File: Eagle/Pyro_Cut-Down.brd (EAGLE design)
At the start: 51.4 x 63.5 mm, 44 parts, among them IC1 ERIC9-FCC, IC2 MCP111T-240E/TT, IC3 SN74LVC2G02DCTR, IC4 MPL3115A2LGA8, Q1 DMG3415U-7, Q2 2N2222

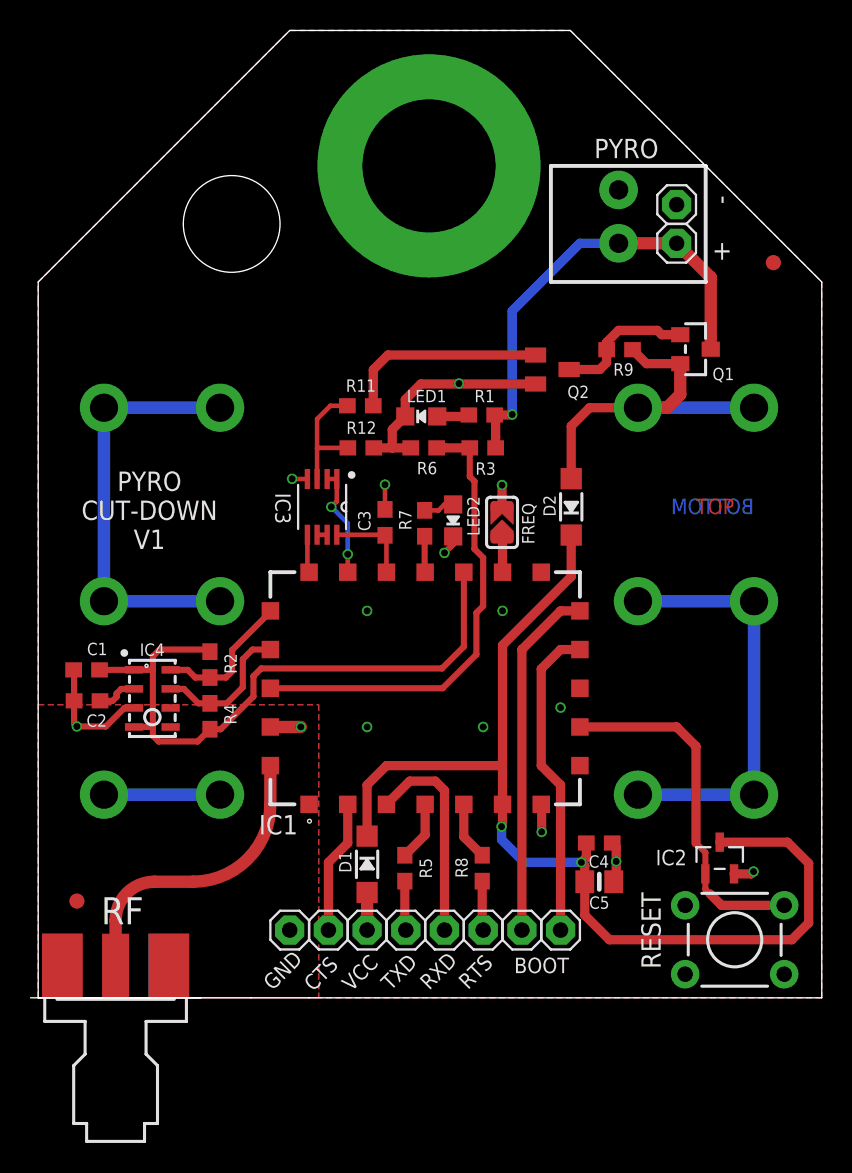
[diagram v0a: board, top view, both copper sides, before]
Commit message: Major update for V2
Major update for V2 of the PCB. Now includes a u-blox CAM-M8Q to provide accurate altitude data. Trigger-at-altitude is now possible.
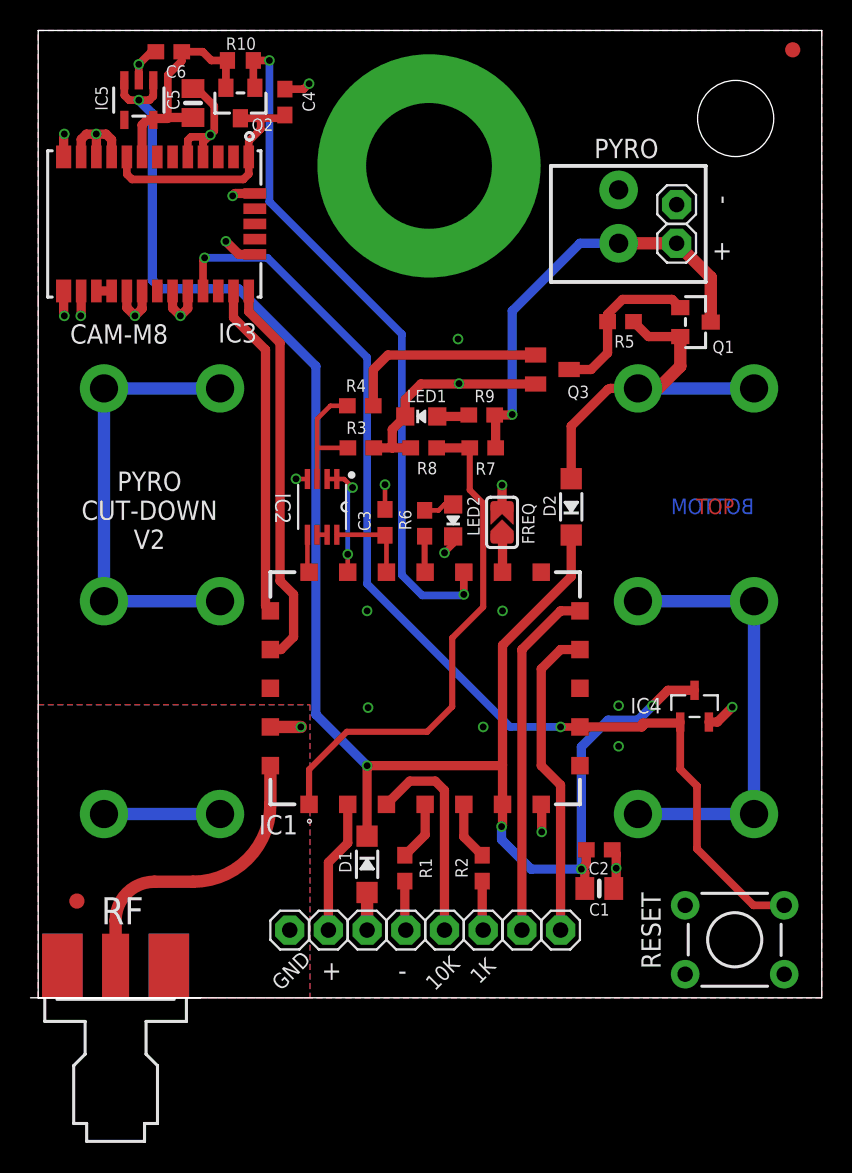
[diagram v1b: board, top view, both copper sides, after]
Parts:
- removed R11: 1K, microbuilder:0603-NO
- removed R12: 10K, microbuilder:0603-NO
- added C6: 100nF, microbuilder:0603-NO
- added IC5: SPX3819-3.3, microbuilder:SOT23-5
- added Q3: 2N2222, transistor:SOT23-BEC
- added R10: 100K, rcl:R0603
- C1: value 1uF -> 10uF; device microbuilder:0603-NO -> microbuilder:0805-NO
- C4: device microbuilder:0603-NO -> rcl:C0603
- C5: value 10uF -> 10µF
- IC2: value MCP111T-240E/TT -> SN74LVC2G02DCTR; device Microchip-MCP11:SOT95P237X112-3N -> SamacSys_Parts:SOP65P400X130-8N
- IC3: value SN74LVC2G02DCTR -> CAM-M8; device SamacSys_Parts:SOP65P400X130-8N -> ubloxLib:CAM-M8
- IC4: value MPL3115A2LGA8 -> MCP111T-240E/TT; device SparkFun-Sensors:LGA8 -> Microchip-MCP11:SOT95P237X112-3N
- Q2: value 2N2222 -> DMG3415U-7; device transistor:SOT23-BEC -> microbuilder:SOT23-WIDE
- R1: value 2.2K -> 1K
- R3: value 100k -> 10K
- R5: value 1K -> 10K
- R6: value 100K -> 1K
- R7: value 1K -> 100k
- R8: value 1K -> 100K
- R9: value 10K -> 2.2K
- moved C5 57.7 mm to (10.2, 58.7), turned to 90 degrees
- moved C4 52.8 mm to (16.2, 58.8), turned to 90 degrees
- moved R5 38.6 mm to (38.2, 44.4), turned to 180 degrees
- moved C1 36.6 mm to (36.8, 7.18), turned to 0 degrees
- moved IC4 35.6 mm to (43.1, 19.1)
- moved C2 35.0 mm to (36.8, 9.72), turned to 0 degrees
- moved IC2 34.8 mm to (18.6, 32.2), turned to 270 degrees
- moved R1 30.2 mm to (24.1, 8.51), turned to 90 degrees
- moved R8 27.9 mm to (25.3, 36.1), turned to 180 degrees
- moved Q2 26.9 mm to (13.3, 58.7), turned to 180 degrees
- moved R4 22.6 mm to (21.1, 38.9), turned to 0 degrees
- moved R2 22.3 mm to (29.1, 8.51), turned to 90 degrees
- moved IC3 21.6 mm to (7.62, 50.8), turned to 180 degrees
- moved FD1 14.0 mm to (49.5, 62.2)
- moved R9 10.0 mm to (29.1, 38.3)
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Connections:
- removed net N$25: C2.1, IC4.2
- removed net RESET: IC1.9, IC2.1, RESET.3
- removed net VBAT: BAT1.PWR@1, BAT1.PWR@2, D2.A, Q1.2, R9.1
- new net !RESET: IC1.9, IC3.23, IC4.1, RESET.3
- new net +3V3: C5.1, C6.1, IC3.8, IC5.5, Q2.2, R10.1
- new net 3V3SW: C4.1, IC3.1, IC3.9, Q2.3
- new net N$8: IC3.16, IC3.17
- new net PIN1: IC1.1, R7.2, R8.1
- new net V+: BAT1.PWR@1, BAT1.PWR@2, D2.A, Q1.2, R5.1
- net FIRE: now also IC2.3, R3.1, R4.1; no longer IC3.3, R11.1, R12.1
- net GND: now also C6.2, IC2.4, IC3.10, IC3.11, IC3.12, IC3.13, IC3.14, IC3.15, IC3.18, IC3.19, IC3.21, IC3.22, IC3.27, IC3.31, IC3.5, IC4.2, IC5.2, Q3.E, R3.2, R8.2; no longer IC2.2, IC4.3, Q2.E, R12.2, R6.2
- net N$19: now also Q3.C, R5.2; no longer Q2.C, R9.2
- net N$2: now also R6.2; no longer R7.2
- net N$20: now also Q3.B, R4.2; no longer Q2.B, R11.2
- net N$4: now also R9.2; no longer R1.2
- net N$5: now also R1.1; no longer R5.1
- net N$6: now also IC2.6, IC2.7; no longer IC3.6, IC3.7
- net N$7: now also R2.1; no longer R8.1
- net PIN15: now also Q2.1, R10.2; no longer C1.1, IC4.1, IC4.4, R2.1, R4.1
- net PIN16: now also R6.1; no longer R7.1
- net PIN17: now also IC2.8; no longer IC3.8
- net PIN18: now also IC2.1, IC2.2; no longer IC3.1, IC3.2
- net PIN19: now also IC2.5; no longer IC3.5
- net PIN20: now also IC3.25; no longer IC4.8, R2.2
- net PIN21: now also IC3.26; no longer IC4.7, R4.2
- net PIN22: no longer R3.2, R6.1
- net PYRO: now also R7.1, R9.1; no longer R1.1, R3.1
- net RTS: now also R2.2; no longer R8.2
- net TXD: now also R1.2; no longer R5.2
- net VCC: now also C1.1, C2.1, IC4.3, IC5.1, IC5.3; no longer C4.1, C5.1, IC2.3
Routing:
- net !RESET: track 0.00 -> 71.2 mm, vias 0 -> 2
- net VCC: track 71.6 -> 118.3 mm, vias 2 -> 5
- net PIN1: track 0.00 -> 33.8 mm
- net PIN22: track 30.7 -> 0.00 mm
- net GND: track 43.9 -> 70.7 mm, vias 17 -> 29
- net V+: track 0.00 -> 25.3 mm
- net VBAT: track 24.6 -> 0.00 mm
- net RESET: track 23.4 -> 0.00 mm
- net 3V3SW: track 0.00 -> 16.4 mm
- net PIN21: track 9.48 -> 25.8 mm
- net +3V3: track 0.00 -> 15.4 mm
- net PIN20: track 9.42 -> 22.0 mm
- net PIN15: track 42.7 -> 46.4 mm, vias 0 -> 2
- net N$25: track 2.69 -> 0.00 mm
- net PYRO: track 30.7 -> 28.9 mm
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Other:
- outline, holes or cut-outs redrawn
- board text added: "10K"
- board text added: "1K"
- board text added: "GND"
- board text added: "PYRO CUT-DOWN V2"
- board text removed: "PYRO CUT-DOWN V1"
